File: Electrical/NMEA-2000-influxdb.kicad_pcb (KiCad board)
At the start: 4 copper layers, 149.9 x 71.8 mm, 23 parts, among them J1 Conn_01x04, J2 Conn_01x04, J3 Conn_01x02, J4 Conn_02x08, U1 LM7805_TO220, U2 ESP32_NODEMCU, U3 SD-Card-Module, U4 SN65HVD230, U5 SN65HVD230-Module

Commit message: Updated PCB
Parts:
- added C3: 0.1uF, Capacitor_THT:C_Disc_D9.0mm_W5.0mm_P7.50mm, F.Cu at (101.9, 97.2)
- added C4: 0.1uF, Capacitor_THT:C_Disc_D9.0mm_W5.0mm_P7.50mm, F.Cu at (101.9, 105.4)
- added H1: MountingHole_Pad, MountingHole:MountingHole_3mm_Pad_Via, F.Cu at (101.2, 122.6)
- added H2: MountingHole_Pad, MountingHole:MountingHole_3mm_Pad_Via, F.Cu at (101.2, 62.6)
- added H3: MountingHole_Pad, MountingHole:MountingHole_3mm_Pad_Via, F.Cu at (216.2, 62.6)
- added H4: MountingHole_Pad, MountingHole:MountingHole_3mm_Pad_Via, F.Cu at (216.2, 122.6)
- C1: value 0.33uF -> 0.1uF
- moved J3 23.8 mm to (85.5, 73.5), turned to 90 degrees
- moved C1 7.49 mm to (101.9, 88.8)
- moved U1 4.61 mm to (93.3, 92.6)
- moved C2 4.00 mm to (90.8, 105.4)
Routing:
- net /CS: track 58.2 -> 104.1 mm
- net +5V: track 136.8 -> 97.8 mm
- net /CAN_RX: track 50.0 -> 84.4 mm, vias 1 -> 0
- net GND: track 159.6 -> 128.1 mm
- net /SW_TG: track 76.1 -> 103.5 mm
- net /SD_ST: track 74.3 -> 90.3 mm
- net +12V: track 229.0 -> 239.9 mm
- net /MOSI: track 54.0 -> 64.3 mm
- net /GREEN: track 78.3 -> 87.8 mm
- net +3V3: track 106.9 -> 114.9 mm
- net /CAN_H: track 144.1 -> 137.6 mm
- net /MISO: track 58.5 -> 63.7 mm
- net /SW_CY: track 82.2 -> 87.2 mm
- net /CAN_L: track 150.7 -> 154.0 mm
- net /SCL: track 93.7 -> 95.9 mm
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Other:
- board size 149.9 x 71.8 mm -> 149.9 x 70 mm

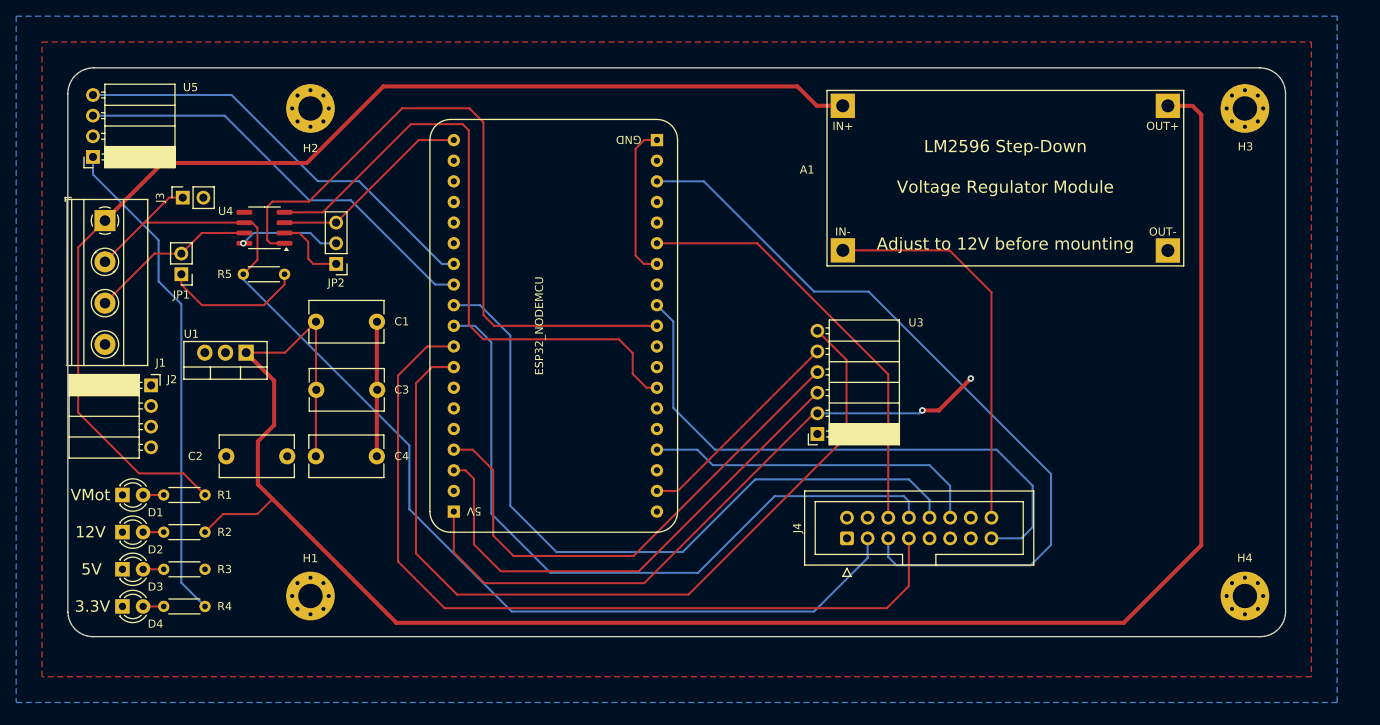
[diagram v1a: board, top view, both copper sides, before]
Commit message: Added SMD SD-Card
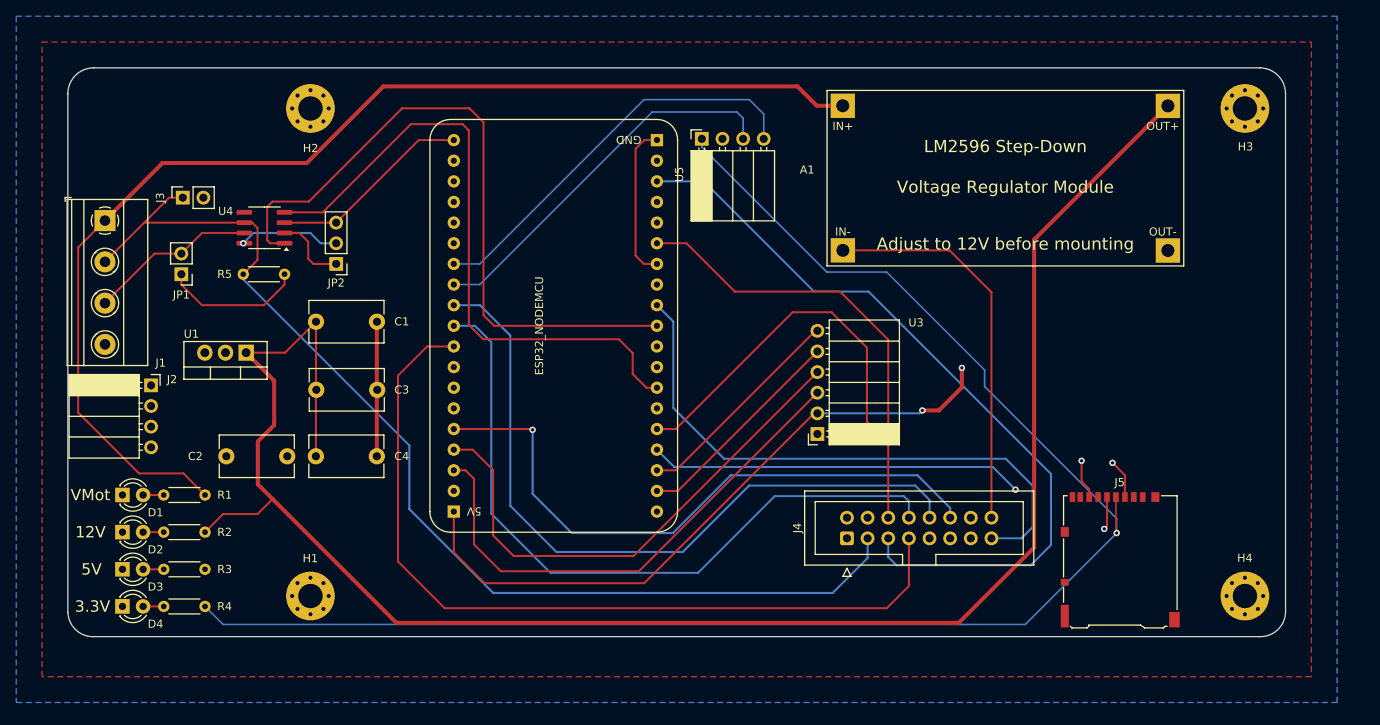
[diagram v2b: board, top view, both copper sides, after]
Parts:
- added J5: Micro_SD_Card, Connector_Card:microSD_HC_Hirose_DM3AT-SF-PEJM5, F.Cu at (200.8, 118.1)
- moved U5 75.0 mm to (149.4, 66.3), turned to 90 degrees
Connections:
- U2 pad 22: unconnected-(U2-SD1-Pad22) -> /CS
- U2 pad 23: /WIFI_ST -> /CMD
- U2 pad 24: unconnected-(U2-G2-Pad24) -> /DAT0
- U2 pad 5: unconnected-(U2-G13-Pad5) -> /WIFI_ST
- U2 pad 8: /CS -> /CLK
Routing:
- net +3.3V: track 61.0 -> 196.2 mm, vias 0 -> 1
- net /CLK: track 0.00 -> 101.8 mm, vias 0 -> 1
- net /CS: track 104.1 -> 26.9 mm
- net /DAT0: track 0.00 -> 76.0 mm, vias 0 -> 2
- net /CMD: track 0.00 -> 64.3 mm, vias 0 -> 2
- net /WIFI_ST: track 41.9 -> 76.8 mm, vias 0 -> 1
- net +12V: track 239.9 -> 222.8 mm
- net /CAN_RX_B: track 53.0 -> 47.3 mm
- net +3V3: track 114.9 -> 119.2 mm
- net /GREEN: track 87.8 -> 91.3 mm
- net /CAN_L: track 154.0 -> 157.1 mm
- net /CAN_ST: track 73.4 -> 70.5 mm
- net /CAN_TX_B: track 53.0 -> 50.3 mm
- net /SDA: track 52.8 -> 55.3 mm
- net /CAN_H: track 137.6 -> 135.7 mm
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
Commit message: Updated 3d Models and PCB
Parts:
- added JP3: Jumper_3_Bridged12, Connector_PinHeader_2.54mm:PinHeader_1x03_P2.54mm_Vertical, F.Cu at (113.6, 82.4)
- added R6: 10k, Resistor_THT:R_Axial_DIN0204_L3.6mm_D1.6mm_P5.08mm_Horizontal, F.Cu at (117.3, 74.8)
- U5: footprint Connector_PinSocket_2.54mm:PinSocket_1x04_P2.54mm_Horizontal -> Connector_PinSocket_2.54mm:PinSocket_1x04_P2.54mm_Vertical
- moved J1 9.82 mm to (79.2, 67.1)
- moved H3 3.33 mm to (219.4, 63.3)
- moved C3 3.33 mm to (105.2, 97.9)
- moved H4 3.33 mm to (219.4, 123.3)
- moved J4 3.33 mm to (170.5, 116.2)
- moved J5 3.33 mm to (204.1, 118.8)
- moved R5 3.33 mm to (101.3, 83.7)
- moved U3 3.33 mm to (166.8, 103.4)
- moved C1 3.33 mm to (105.1, 89.5)
- moved C2 3.33 mm to (94.1, 106.1)
- moved C4 3.33 mm to (105.1, 106.1)
- moved D1 3.33 mm to (81.3, 110.9)
- moved D2 3.33 mm to (81.3, 115.4)
- moved D3 3.33 mm to (81.3, 120.0)
- moved D4 3.33 mm to (81.3, 124.6)
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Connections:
- J5 pad 4: +3.3V -> +3V3
- JP2 pad 1: GND -> Net-(JP2-A)
- R4 pad 1: +3.3V -> +3V3
- U5 pad 1: +3.3V -> +3V3
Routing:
- net +3V3: track 119.2 -> 319.5 mm, vias 0 -> 1
- net +3.3V: track 196.2 -> 0.00 mm, vias 1 -> 0
- net GND: track 128.1 -> 215.2 mm, vias 0 -> 3
- net +5V: track 98.6 -> 115.0 mm, vias 2 -> 3
- net /GREEN: track 91.3 -> 103.9 mm
- net VMot: track 143.4 -> 151.7 mm
- net /CAN_H: track 135.7 -> 128.0 mm
- net Net-(JP2-A): track 0.00 -> 6.02 mm
- net /CLK: track 101.8 -> 107.1 mm
- net /WIFI_ST: track 76.8 -> 81.9 mm
- net /SD_ST: track 89.7 -> 94.1 mm
- net /SW_CY: track 87.2 -> 91.0 mm
- net Net-(JP3-C): track 0.00 -> 3.68 mm
- net Net-(JP2-C): track 12.6 -> 11.4 mm
- net /MOSI: track 64.3 -> 65.2 mm
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
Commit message: Finished Revision 3
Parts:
- renumbered C3 to C2, C4 to C3, C2 to C4, J5 to J4, J4 to J5, U4 to U3, U5 to U4, U3 to U5

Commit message: Finished Rev 4 Schematics
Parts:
- removed A1: LM2596_Step_Down_Module, LM2596:LM2596_Step_Down_Module-21.3x43.6mm
- added C10: 0.1uF, Capacitor_THT:C_Disc_D5.0mm_W2.5mm_P5.00mm, F.Cu at (142.5, 106.2)
- added C11: 0.1uF, Capacitor_THT:C_Disc_D5.0mm_W2.5mm_P5.00mm, F.Cu at (127.0, 106.2)
- added C5: 0.1uF, Capacitor_THT:C_Disc_D5.0mm_W2.5mm_P5.00mm, F.Cu at (131.6, 85.3)
- added C6: 1uF, Capacitor_THT:C_Disc_D5.0mm_W2.5mm_P5.00mm, F.Cu at (152.1, 77.4)
- added C7: 22uF, Capacitor_THT:C_Radial_D5.0mm_H7.0mm_P2.00mm, F.Cu at (154.9, 91.3)
- added C8: 0.1uF, Capacitor_THT:C_Disc_D5.0mm_W2.5mm_P5.00mm, F.Cu at (148.9, 106.2)
- added C9: 0.1nF, Capacitor_THT:C_Disc_D5.0mm_W2.5mm_P5.00mm, F.Cu at (186.5, 102.0)
- added D5: LED, LED_THT:LED_D3.0mm, F.Cu at (220.4, 79.4)
- added F1: Polyfuse, Diode_SMD:D_1210_3225Metric_Pad1.42x2.65mm_HandSolder, F.Cu at (108.5, 64.8)
- added R10: 330R, Resistor_THT:R_Axial_DIN0204_L3.6mm_D1.6mm_P5.08mm_Horizontal, F.Cu at (208.4, 79.4)
- added R11: 3.3k, Resistor_THT:R_Axial_DIN0204_L3.6mm_D1.6mm_P5.08mm_Horizontal, F.Cu at (185.4, 97.0)
- added R12: 4.7k, Resistor_THT:R_Axial_DIN0204_L3.6mm_D1.6mm_P5.08mm_Horizontal, F.Cu at (170.4, 103.4)
- added R13: 4.7k, Resistor_THT:R_Axial_DIN0204_L3.6mm_D1.6mm_P5.08mm_Horizontal, F.Cu at (170.4, 97.8)
- added R7: 120R, Resistor_THT:R_Axial_DIN0204_L3.6mm_D1.6mm_P5.08mm_Horizontal, F.Cu at (109.7, 89.2)
- added R8: 10k, Resistor_THT:R_Axial_DIN0204_L3.6mm_D1.6mm_P5.08mm_Horizontal, F.Cu at (121.2, 114.2)
- added R9: 10k, Resistor_THT:R_Axial_DIN0204_L3.6mm_D1.6mm_P5.08mm_Horizontal, F.Cu at (185.4, 82.2)
- added SW1: SW_Push, Button_Switch_THT:SW_PUSH_6mm, F.Cu at (131.4, 61.2)
- added TP1: V_{Mot}, TestPoint:TestPoint_Pad_2.5x2.5mm, F.Cu at (204.3, 114.4)
- added TP2: 12V, TestPoint:TestPoint_Pad_2.5x2.5mm, F.Cu at (204.3, 105.7)
- added TP3: 5V, TestPoint:TestPoint_Pad_2.5x2.5mm, F.Cu at (204.3, 96.9)
- added TP4: 3.3V, TestPoint:TestPoint_Pad_2.5x2.5mm, F.Cu at (204.3, 88.2)
- added TP5: EN, TestPoint:TestPoint_Pad_2.5x2.5mm, F.Cu at (137.4, 71.8)
- C1: value 0.1uF -> 0.33uF; footprint Capacitor_THT:C_Disc_D9.0mm_W5.0mm_P7.50mm -> Capacitor_THT:C_Disc_D5.0mm_W2.5mm_P5.00mm
- C2: footprint Capacitor_THT:C_Disc_D9.0mm_W5.0mm_P7.50mm -> Capacitor_THT:C_Disc_D5.0mm_W2.5mm_P5.00mm
- C3, C4: value 0.1uF -> 22uF; footprint Capacitor_THT:C_Disc_D9.0mm_W5.0mm_P7.50mm -> Capacitor_THT:C_Radial_D5.0mm_H7.0mm_P2.00mm
- J1: footprint TerminalBlock_Phoenix:TerminalBlock_Phoenix_MKDS-1,5-4-5.08_1x04_P5.08mm_Horizontal -> TerminalBlock_Phoenix:TerminalBlock_Phoenix_PT-1,5-4-5.0-H_1x04_P5.00mm_Horizontal
- J3: value Conn_01x02 -> Conn_01x04; footprint Connector_PinSocket_2.54mm:PinSocket_1x02_P2.54mm_Vertical -> Connector:FanPinHeader_1x04_P2.54mm_Vertical
- R5: value 120R -> 0R
- U2: value ESP32_NODEMCU -> AMS1117-3.3; footprint esp32:esp32 -> Package_TO_SOT_SMD:SOT-223-3_TabPin2
- U4: value SN65HVD230-Module -> ESP32-WROOM-32E; footprint Connector_PinSocket_2.54mm:PinSocket_1x04_P2.54mm_Vertical -> RF_Module:ESP32-WROOM-32D
- U5: value SD-Card-Module -> BME280; footprint Connector_PinSocket_2.54mm:PinSocket_1x06_P2.54mm_Horizontal -> Package_LGA:Bosch_LGA-8_2.5x2.5mm_P0.65mm_ClockwisePinNumbering
- moved D4 143.8 mm to (220.4, 88.2), turned to 180 degrees
- moved D3 141.0 mm to (220.4, 96.9), turned to 180 degrees
- moved D2 139.5 mm to (220.4, 105.7), turned to 180 degrees
- moved D1 139.2 mm to (220.4, 114.4), turned to 180 degrees
- moved H3 134.2 mm to (99.4, 123.3)
- moved R4 122.5 mm to (208.4, 88.2), turned to 0 degrees
- moved H2 120.0 mm to (219.4, 63.3)
- moved R3 119.2 mm to (208.4, 96.9), turned to 0 degrees
- moved R2 117.4 mm to (208.4, 105.7), turned to 0 degrees
- moved R1 117.0 mm to (208.4, 114.4), turned to 0 degrees
- moved J3 106.3 mm to (192.8, 95.8)
- moved H1 60.0 mm to (99.4, 63.3)
- moved C4 57.0 mm to (149.1, 91.3), turned to -90 degrees
- moved J2 56.4 mm to (137.3, 118.1), turned to 90 degrees
- moved J4 51.1 mm to (203.4, 67.7), turned to 180 degrees
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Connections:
- C2 pad 1: +12V -> +5V
- C3 pad 1: +12V -> +5V
- C4 pad 1: +5V -> +3.3V
- J2 pad 2: /RX -> /TX
- J2 pad 3: /TX -> /RX
- J3 pad 1: /CAN_H -> GND
- J3 pad 2: /CAN_L -> +12V
- J4 pad 4: +3V3 -> +3.3V
- J5 pad 2: +3V3 -> +3.3V
- JP2 pad 3: +3V3 -> +3.3V
- R4 pad 1: +3V3 -> +3.3V
- R5 pad 1: Net-(JP1-A) -> Net-(C5-Pad2)
- R5 pad 2: /CAN_H -> /EN
- R6 pad 1: GND -> /EN
- R6 pad 2: Net-(JP3-C) -> +3.3V
- U2 pad 1: +5V -> GND
- U2 pad 2: unconnected-(U2-CMD-Pad2) -> +3.3V
- U2 pad 3: /MISO -> +5V
- U3 pad 3: +3V3 -> +3.3V
- U4 pad 1: +3V3 -> GND
- U4 pad 2: GND -> +3.3V
- U4 pad 3: /CAN_RX_B -> /EN
- U4 pad 4: /CAN_TX_B -> unconnected-(U4-SENSOR_VP-Pad4)
- U5 pad 2: +5V -> +3.3V
- U5 pad 3: /MISO -> /SDA
- U5 pad 4: /MOSI -> /SCL
- U5 pad 5: /SCK -> GND
- U5 pad 6: /CS -> +3.3V
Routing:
- net +3V3: track 319.5 -> 0.00 mm, vias 1 -> 0
- net GND: track 215.2 -> 90.3 mm, vias 3 -> 1
- net +12V: track 222.8 -> 135.6 mm
- net /MOSI: track 65.2 -> 0.00 mm
- net /MISO: track 63.7 -> 0.00 mm
- net /SW_TG: track 103.5 -> 43.2 mm, vias 0 -> 2
- net /CLK: track 107.1 -> 50.1 mm, vias 1 -> 2
- net /TX: track 119.7 -> 65.7 mm, vias 0 -> 1
- net Net-(U4-IO32): track 0.00 -> 53.3 mm, vias 0 -> 1
- net +3.3V: track 0.00 -> 53.0 mm, vias 0 -> 1
- net /GREEN: track 103.9 -> 51.1 mm, vias 0 -> 1
- net /CAN_TX_B: track 50.9 -> 0.00 mm
- net /RX: track 104.6 -> 55.6 mm
- net /CAN_RX_B: track 47.9 -> 0.00 mm
- net +5V: track 115.0 -> 161.4 mm, vias 3 -> 0
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- added copper zone on F.Cu, net +3.3V
- added copper zone on B.Cu, net GND
- removed copper zone on B.Cu, net +5V
- removed copper zone on F.Cu, net GND
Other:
- board size 149.9 x 70 mm -> 129.9 x 70 mm

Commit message: Finished Rev 4
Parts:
- removed the C10 at (142.5, 106.2)
- removed the C11 at (127.0, 106.2)
- removed the D5 at (220.4, 79.4)
- removed R11: 3.3k, Resistor_THT:R_Axial_DIN0204_L3.6mm_D1.6mm_P5.08mm_Horizontal
- removed R12, R13: 4.7k, Resistor_THT:R_Axial_DIN0204_L3.6mm_D1.6mm_P5.08mm_Horizontal
- removed the R5 at (147.1, 81.7)
- removed the U4 at (171.1, 83.4)
- removed the U5 at (163.1, 100.8)
- added C3: 0.1uF, Capacitor_THT:C_Disc_D5.0mm_W2.5mm_P5.00mm, F.Cu at (160.5, 103.9)
- added C4: 22uF, Capacitor_THT:C_Radial_D4.0mm_H7.0mm_P1.50mm, F.Cu at (138.2, 85.6)
- added D2: LED, LED_THT:LED_D3.0mm, F.Cu at (220.5, 117.1)
- added J4: Conn_01x03, Connector_PinHeader_2.54mm:PinHeader_1x03_P2.54mm_Vertical, F.Cu at (151.6, 124.7)
- added JP1: Jumper_2_Open, Connector_PinHeader_2.54mm:PinHeader_1x02_P2.54mm_Vertical, F.Cu at (107.2, 70.1)
- added R7: 1.2k, Resistor_THT:R_Axial_DIN0207_L6.3mm_D2.5mm_P10.16mm_Horizontal, F.Cu at (205.0, 109.2)
- added U1: BMP280, Package_LGA:Bosch_LGA-8_2x2.5mm_P0.65mm_ClockwisePinNumbering, F.Cu at (160.6, 99.9)
- added U3: ESP32-WROOM-32E, RF_Module:ESP32-WROOM-32D, F.Cu at (171.2, 83.5)
- C1: value 0.33uF -> 0.1uF
- C10: renamed from C3; footprint Capacitor_THT:C_Radial_D5.0mm_H7.0mm_P2.00mm -> Capacitor_THT:C_Radial_D4.0mm_H7.0mm_P1.50mm
- C11: renamed from C4; footprint Capacitor_THT:C_Radial_D5.0mm_H7.0mm_P2.00mm -> Capacitor_THT:C_Radial_D4.0mm_H7.0mm_P1.50mm
- C2: value 0.1uF -> 0.1nF
- C6: value 1uF -> 0.1uF
- C7: value 22uF -> 0.33uF; footprint Capacitor_THT:C_Radial_D5.0mm_H7.0mm_P2.00mm -> Capacitor_THT:C_Disc_D5.0mm_W2.5mm_P5.00mm
- C9: value 0.1nF -> 0.1uF
- D1: value LED -> LED_Small
- R1: value 1.5k -> 10k; footprint Resistor_THT:R_Axial_DIN0204_L3.6mm_D1.6mm_P5.08mm_Horizontal -> Resistor_THT:R_Axial_DIN0207_L6.3mm_D2.5mm_P10.16mm_Horizontal
- R10, R4: footprint Resistor_THT:R_Axial_DIN0204_L3.6mm_D1.6mm_P5.08mm_Horizontal -> Resistor_THT:R_Axial_DIN0207_L6.3mm_D2.5mm_P10.16mm_Horizontal
- R2: value 1.2k -> 3.3k; footprint Resistor_THT:R_Axial_DIN0204_L3.6mm_D1.6mm_P5.08mm_Horizontal -> Resistor_THT:R_Axial_DIN0207_L6.3mm_D2.5mm_P10.16mm_Horizontal
- R3: value 500R -> 10k; footprint Resistor_THT:R_Axial_DIN0204_L3.6mm_D1.6mm_P5.08mm_Horizontal -> Resistor_THT:R_Axial_DIN0207_L6.3mm_D2.5mm_P10.16mm_Horizontal
- R5: renamed from R8; footprint Resistor_THT:R_Axial_DIN0204_L3.6mm_D1.6mm_P5.08mm_Horizontal -> Resistor_THT:R_Axial_DIN0207_L6.3mm_D2.5mm_P10.16mm_Horizontal
- R6: value 10k -> 1.5k; footprint Resistor_THT:R_Axial_DIN0204_L3.6mm_D1.6mm_P5.08mm_Horizontal -> Resistor_THT:R_Axial_DIN0207_L6.3mm_D2.5mm_P10.16mm_Horizontal
- R8: renamed from R7; footprint Resistor_THT:R_Axial_DIN0204_L3.6mm_D1.6mm_P5.08mm_Horizontal -> Resistor_THT:R_Axial_DIN0207_L6.3mm_D2.5mm_P10.16mm_Horizontal
- R9: value 10k -> 500R; footprint Resistor_THT:R_Axial_DIN0204_L3.6mm_D1.6mm_P5.08mm_Horizontal -> Resistor_THT:R_Axial_DIN0207_L6.3mm_D2.5mm_P10.16mm_Horizontal
- moved R2 102.2 mm to (107.2, 119.4), turned to 90 degrees
- moved R1 96.3 mm to (112.3, 109.2), turned to -90 degrees
- moved J3 94.9 mm to (99.8, 114.3)
- moved R3 65.6 mm to (146.3, 75.7)
- moved R6 61.4 mm to (205.0, 117.1), turned to 0 degrees
- moved C2 54.9 mm to (107.2, 123.4), turned to 0 degrees
- moved C1 51.6 mm to (160.5, 109.0), turned to 180 degrees
- moved C9 49.4 mm to (137.3, 106.2)
- moved C7 38.6 mm to (118.2, 79.5), turned to 0 degrees
- moved D1 31.6 mm to (220.5, 82.8)
- moved R9 26.5 mm to (204.7, 100.3), turned to 0 degrees
- moved C8 21.8 mm to (154.2, 85.0), turned to 90 degrees
- moved C6 18.2 mm to (134.1, 79.5)
- moved C5 15.9 mm to (147.6, 85.0), turned to 90 degrees
- moved R10 11.7 mm to (205.2, 90.7)
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- renumbered D2 to D3, D3 to D4, D4 to D5, J4 to J6, JP1 to JP4, U1 to U2, U2 to U4, U3 to U5
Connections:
- C1 pad 1: +12V -> +3.3V
- C2 pad 1: +5V -> /TACHO
- C5 pad 2: Net-(C5-Pad2) -> /EN
- C6 pad 1: GND -> +3.3V
- C6 pad 2: /EN -> GND
- C7 pad 1: +3.3V -> +12V
- C8 pad 1: +3.3V -> GND
- C8 pad 2: GND -> /EN
- C9 pad 1: Net-(U4-IO34) -> +5V
- D3 pad 2: Net-(D2-A) -> Net-(D3-A)
- D4 pad 2: Net-(D3-A) -> Net-(D4-A)
- D5 pad 2: Net-(D4-A) -> Net-(D5-A)
- J3 pad 3: /TACHO -> Net-(J3-Pin_3)
- R1 pad 1: VMot -> Net-(J3-Pin_3)
- R1 pad 2: Net-(D1-A) -> +3.3V
- R10 pad 1: Net-(U4-IO32) -> +3.3V
- R2 pad 1: +12V -> /TACHO
- R2 pad 2: Net-(D2-A) -> Net-(J3-Pin_3)
- R3 pad 1: +5V -> /EN
- R3 pad 2: Net-(D3-A) -> +3.3V
- R4 pad 1: +3.3V -> Net-(U3-IO32)
- R4 pad 2: Net-(D4-A) -> Net-(D1-A)
- R6 pad 1: /EN -> VMot
- R6 pad 2: +3.3V -> Net-(D2-A)
- R9 pad 1: +3.3V -> +5V
- R9 pad 2: /TACHO -> Net-(D4-A)
- SW1 pad 2: Net-(C5-Pad2) -> /EN
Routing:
- net +3.3V: track 53.0 -> 157.1 mm, vias 1 -> 10
- net /IO0: track 0.00 -> 73.0 mm, vias 0 -> 1
- net /TACHO: track 12.5 -> 76.8 mm, vias 0 -> 1
- net Net-(U3-IO32): track 0.00 -> 57.5 mm, vias 0 -> 1
- net Net-(U4-IO32): track 53.3 -> 0.00 mm, vias 1 -> 0
- net +12V: track 135.6 -> 188.4 mm
- net /PWM: track 31.9 -> 80.8 mm
- net /IO35: track 0.00 -> 47.5 mm, vias 0 -> 1
- net Net-(U4-IO34): track 41.8 -> 0.00 mm, vias 1 -> 0
- net /IO12: track 0.00 -> 38.6 mm, vias 0 -> 1
- net Net-(C5-Pad2): track 38.2 -> 0.00 mm
- net +5V: track 161.4 -> 147.7 mm
- net Net-(J3-Pin_3): track 0.00 -> 12.5 mm
- net /EN: track 34.8 -> 45.1 mm
- net VMot: track 175.5 -> 185.2 mm, vias 1 -> 0
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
